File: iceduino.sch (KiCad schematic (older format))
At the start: 7 parts, among them U1 ICE40HX4K-TQ144

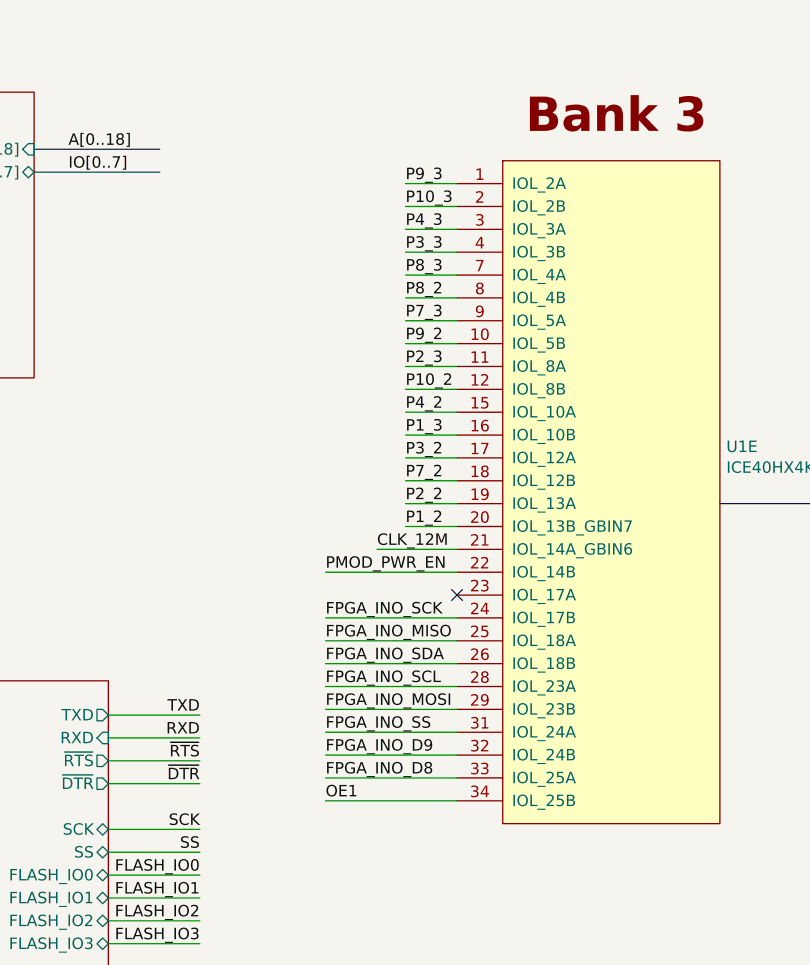
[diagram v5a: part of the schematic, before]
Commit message: FPGA PINs for PMOD reorganized FPGA PINs for Arduino Header reorganized Trace routing partially ready
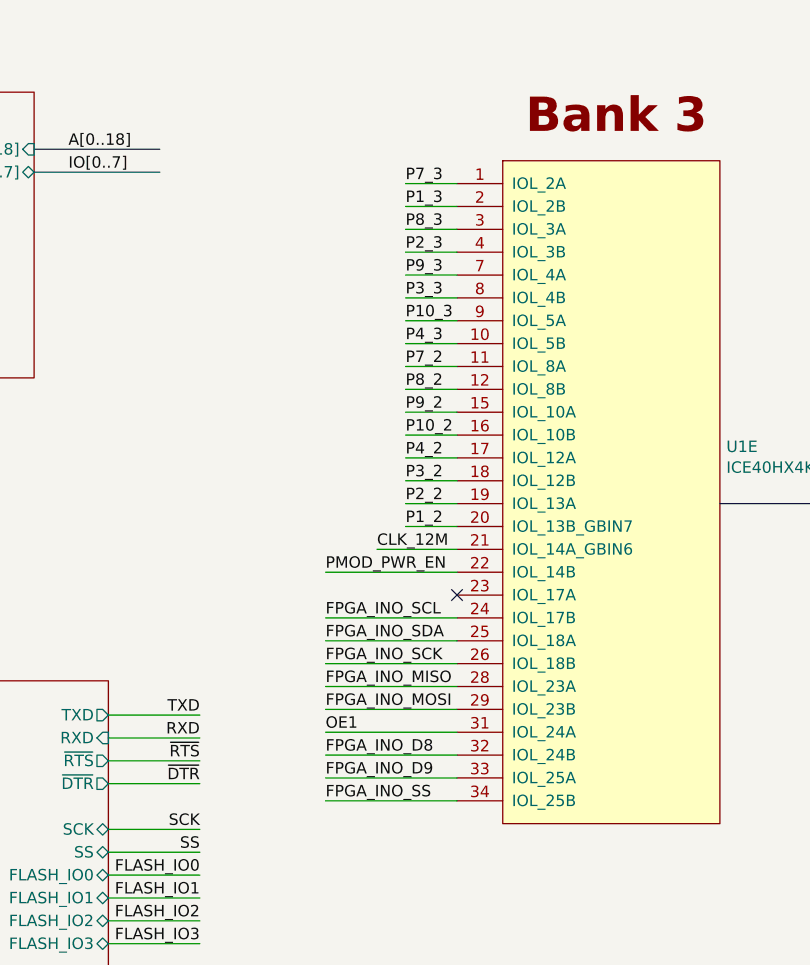
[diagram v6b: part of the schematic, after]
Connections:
- net FPGA_INO_D8: now also U1.32 (IOL_24B); no longer U1.33 (IOL_25A)
- net FPGA_INO_D9: now also U1.33 (IOL_25A); no longer U1.32 (IOL_24B)
- net FPGA_INO_MISO: now also U1.28 (IOL_23A); no longer U1.25 (IOL_18A)
- net FPGA_INO_SCK: now also U1.26 (IOL_18B); no longer U1.24 (IOL_17B)
- net FPGA_INO_SCL: now also U1.24 (IOL_17B); no longer U1.28 (IOL_23A)
- net FPGA_INO_SDA: now also U1.25 (IOL_18A); no longer U1.26 (IOL_18B)
- net FPGA_INO_SS: now also U1.34 (IOL_25B); no longer U1.31 (IOL_24A)
- net OE1: now also U1.31 (IOL_24A); no longer U1.34 (IOL_25B)
- net P10_2: now also U1.16 (IOL_10B); no longer U1.12 (IOL_8B)
- net P10_3: now also U1.9 (IOL_5A); no longer U1.2 (IOL_2B)
- net P1_3: now also U1.2 (IOL_2B); no longer U1.16 (IOL_10B)
- net P2_3: now also U1.4 (IOL_3B); no longer U1.11 (IOL_8A)
- net P3_2: now also U1.18 (IOL_12B); no longer U1.17 (IOL_12A)
- net P3_3: now also U1.8 (IOL_4B); no longer U1.4 (IOL_3B)
- net P4_2: now also U1.17 (IOL_12A); no longer U1.15 (IOL_10A)
- net P4_3: now also U1.10 (IOL_5B); no longer U1.3 (IOL_3A)
- net P7_2: now also U1.11 (IOL_8A); no longer U1.18 (IOL_12B)
- net P7_3: now also U1.1 (IOL_2A); no longer U1.9 (IOL_5A)
- net P8_2: now also U1.12 (IOL_8B); no longer U1.8 (IOL_4B)
- net P8_3: now also U1.3 (IOL_3A); no longer U1.7 (IOL_4A)
- net P9_2: now also U1.15 (IOL_10A); no longer U1.10 (IOL_5B)
- net P9_3: now also U1.7 (IOL_4A); no longer U1.1 (IOL_2A)
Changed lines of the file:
@@
 Wire Wire Line
 	4775 5650 5000 5650
-Text Label 4775 5450 0    50   ~ 0
+Text Label 4775 5550 0    50   ~ 0
 P3_2
 Wire Wire Line
 	4775 5450 5000 5450
-Text Label 4775 5250 0    50   ~ 0
+Text Label 4775 5450 0    50   ~ 0
 P4_2
 Wire Wire Line
 	4775 5250 5000 5250
-Text Label 4775 5550 0    50   ~ 0
+Text Label 4775 5050 0    50   ~ 0
 P7_2
 Wire Wire Line
 	4775 5550 5000 5550
-Text Label 4775 4750 0    50   ~ 0
+Text Label 4775 5150 0    50   ~ 0
 P8_2
 Wire Wire Line
 	4775 4750 5000 4750
-Text Label 4775 4950 0    50   ~ 0
+Text Label 4775 5250 0    50   ~ 0
 P9_2
 Wire Wire Line
 	4775 4950 5000 4950
-Text Label 4775 5350 0    50   ~ 0
+Text Label 4775 4350 0    50   ~ 0
 P1_3
 Wire Wire Line
 	4775 5350 5000 5350
-Text Label 4775 5050 0    50   ~ 0
+Text Label 4775 4550 0    50   ~ 0
 P2_3
 Wire Wire Line
 	4775 5050 5000 5050
-Text Label 4775 4550 0    50   ~ 0
+Text Label 4775 4750 0    50   ~ 0
 P3_3
 Wire Wire Line
 	4775 4550 5000 4550
-Text Label 4775 4450 0    50   ~ 0
+Text Label 4775 4950 0    50   ~ 0
 P4_3
 Wire Wire Line
 	4775 4450 5000 4450
-Text Label 4775 4850 0    50   ~ 0
+Text Label 4775 4250 0    50   ~ 0
 P7_3
 Wire Wire Line
 	4775 4850 5000 4850
-Text Label 4775 4650 0    50   ~ 0
+Text Label 4775 4450 0    50   ~ 0
 P8_3
 Wire Wire Line
 	4775 4650 5000 4650
-Text Label 4775 4250 0    50   ~ 0
+Text Label 4775 4650 0    50   ~ 0
 P9_3
 Wire Wire Line
 	4775 4250 5000 4250
-Text Label 4775 4350 0    50   ~ 0
+Text Label 4775 4850 0    50   ~ 0
 P10_3
 Wire Wire Line
@@
 Wire Wire Line
 	4425 6150 5000 6150
-Text Label 4425 6150 0    50   ~ 0
+Text Label 4425 6350 0    50   ~ 0
 FPGA_INO_SCK
 Wire Wire Line
 	4425 6250 5000 6250
-Text Label 4425 6250 0    50   ~ 0
+Text Label 4425 6450 0    50   ~ 0
 FPGA_INO_MISO
 Wire Wire Line
@@
 Wire Wire Line
 	4425 6650 5000 6650
-Text Label 4425 6650 0    50   ~ 0
+Text Label 4425 6950 0    50   ~ 0
 FPGA_INO_SS
 Wire Wire Line
 	4425 6750 5000 6750
-Text Label 4425 6750 0    50   ~ 0
+Text Label 4425 6850 0    50   ~ 0
 FPGA_INO_D9
 Wire Wire Line
 	4425 6850 5000 6850
-Text Label 4425 6850 0    50   ~ 0
+Text Label 4425 6750 0    50   ~ 0
 FPGA_INO_D8
 Wire Wire Line
 	4425 6450 5000 6450
-Text Label 4425 6450 0    50   ~ 0
+Text Label 4425 6150 0    50   ~ 0
 FPGA_INO_SCL
 Wire Wire Line
 	4425 6350 5000 6350
-Text Label 4425 6350 0    50   ~ 0
+Text Label 4425 6250 0    50   ~ 0
 FPGA_INO_SDA
 Wire Wire Line
 	4425 6950 5000 6950
-Text Label 4425 6950 0    50   ~ 0
+Text Label 4425 6650 0    50   ~ 0
 OE1
 Wire Wire Line
 	4775 5150 5000 5150
-Text Label 4775 5150 0    50   ~ 0
+Text Label 4775 5350 0    50   ~ 0
 P10_2
 Text Label 4425 5950 0    50   ~ 0

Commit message: Board design completed Revision 1
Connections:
- net FPGA_INO_MISO: now also U1.26 (IOL_18B); no longer U1.28 (IOL_23A)
- net FPGA_INO_RX: now also U1.37 (IOB_56); no longer U1.38 (IOB_57)
- net FPGA_INO_SCK: now also U1.28 (IOL_23A); no longer U1.26 (IOL_18B)
- net FPGA_INO_TX: now also U1.38 (IOB_57); no longer U1.37 (IOB_56)
- net P10_1: now also U1.141 (IOT_219); no longer U1.137 (IOT_215)
- net P1_1: now also U1.136 (IOT_214); no longer U1.143 (IOT_221)
- net P2_1: now also U1.144 (IOT_222); no longer U1.141 (IOT_219)
- net P3_1: now also U1.143 (IOT_221); no longer U1.138 (IOT_216)
- net P4_1: now also U1.142 (IOT_220); no longer U1.136 (IOT_214)
- net P7_1: now also U1.137 (IOT_215); no longer U1.144 (IOT_222)
- net P8_1: now also U1.138 (IOT_216); no longer U1.142 (IOT_220)
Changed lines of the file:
@@
 Wire Wire Line
 	4425 6150 5000 6150
+Text Label 4425 6450 0    50   ~ 0
+FPGA_INO_SCK
+Wire Wire Line
+	4425 6250 5000 6250
 Text Label 4425 6350 0    50   ~ 0
-FPGA_INO_SCK
-Wire Wire Line
-	4425 6250 5000 6250
-Text Label 4425 6450 0    50   ~ 0
 FPGA_INO_MISO
 Wire Wire Line
@@
 Text Label 15550 4550 2    50   ~ 0
 P9_2
+Text Label 7650 2650 3    50   ~ 0
+P7_1
+Text Label 7750 2650 3    50   ~ 0
+P1_1
+Text Label 7550 2650 3    50   ~ 0
+P8_1
 Text Label 7050 2650 3    50   ~ 0
-P7_1
-Text Label 7150 2650 3    50   ~ 0
-P1_1
-Text Label 7250 2650 3    50   ~ 0
-P8_1
-Text Label 7350 2650 3    50   ~ 0
 P2_1
 Text Label 7450 2650 3    50   ~ 0
 P9_1
-Text Label 7550 2650 3    50   ~ 0
+Text Label 7150 2650 3    50   ~ 0
 P3_1
-Text Label 7650 2650 3    50   ~ 0
+Text Label 7350 2650 3    50   ~ 0
 P10_1
-Text Label 7750 2650 3    50   ~ 0
+Text Label 7250 2650 3    50   ~ 0
 P4_1
 $Comp
@@
 Wire Wire Line
 	6250 9475 6250 8900
+Text Label 6350 9475 1    50   ~ 0
+FPGA_INO_TX
+Wire Wire Line
+	6350 9475 6350 8900
 Text Label 6250 9475 1    50   ~ 0
-FPGA_INO_TX
-Wire Wire Line
-	6350 9475 6350 8900
-Text Label 6350 9475 1    50   ~ 0
 FPGA_INO_RX
 Wire Wire Line
